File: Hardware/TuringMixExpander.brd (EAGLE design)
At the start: 99 x 50.3 mm, 35 parts, among them IC1 TL074P, IC2 TL072P

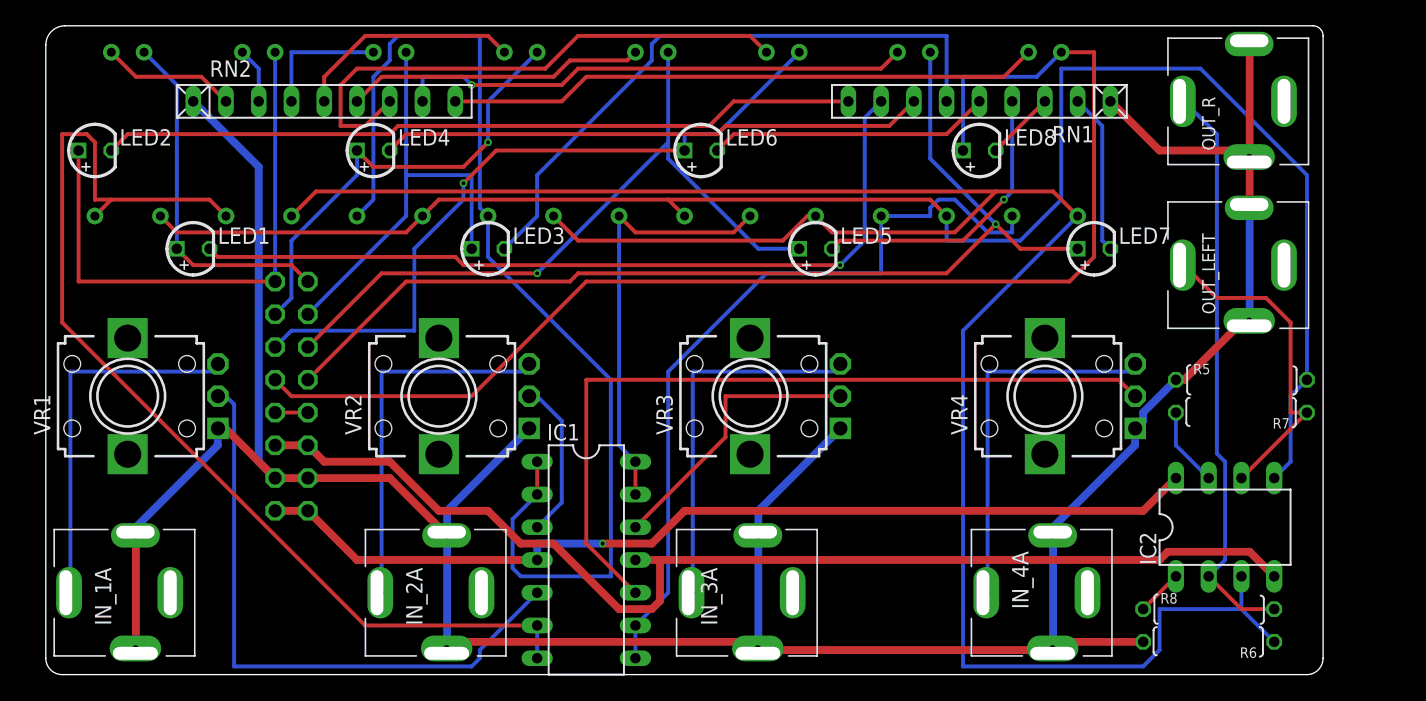
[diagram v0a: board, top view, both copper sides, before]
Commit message: New pcb layout
Added passthrough header
Removed resistor networks
Simplified led/resistor structure (one per channel, not two)
New panel layout
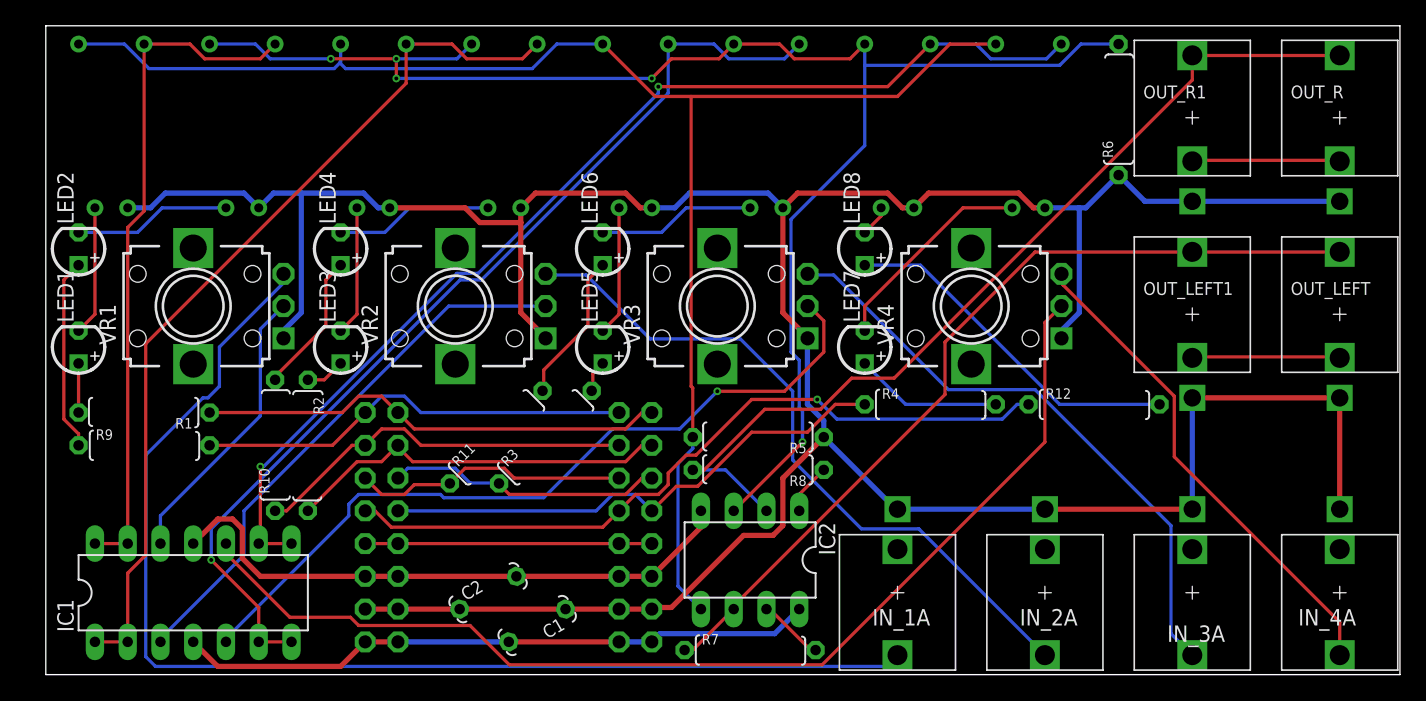
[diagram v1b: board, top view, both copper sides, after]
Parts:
- removed RN1, RN2: 2.2k, resistor-net:RN-9
- added C1, C2: 100n, TomW:C050-024X044
- added GATES1: (no value), con-lstb:MA08-2
- added OUT_LEFT1, OUT_R1: THONKICONN, TomW:THONKICONN
- added R1, R10, R11, R12, R2, R3, R4, R9: 2K, TomW:0207/10
- IN_1A, IN_2A, IN_3A, IN_4A, OUT_LEFT, OUT_R: value ERTHENVAR_SLIMLINE -> THONKICONN; device TomW:ERTHENVAR_SLIMLINE -> TomW:THONKICONN
- moved IN_1A 59.7 mm to (66.0, 6.35), turned to 180 degrees
- moved IN_2A 47.0 mm to (77.5, 6.35), turned to 180 degrees
- moved R7 42.3 mm to (54.6, 1.91), turned to 0 degrees
- moved R6 41.9 mm to (83.2, 43.8), turned to 90 degrees
- moved R5 37.7 mm to (55.2, 18.4), turned to 180 degrees
- moved IC2 36.9 mm to (54.6, 8.89), turned to 180 degrees
- moved R8 36.6 mm to (55.2, 15.9), turned to 180 degrees
- moved IN_3A 34.3 mm to (88.9, 6.35), turned to 180 degrees
- moved IC1 30.6 mm to (11.4, 6.35), turned to 0 degrees
- moved GATES 28.5 mm to (45.7, 11.4)
- moved IN_4A 22.9 mm to (100.3, 6.35), turned to 180 degrees
- moved LED7 19.3 mm to (63.5, 25.4), turned to 90 degrees
- moved LED5 18.2 mm to (43.2, 25.4), turned to 90 degrees
- moved LED3 13.7 mm to (22.9, 25.4), turned to 90 degrees
- moved LED1 11.7 mm to (2.54, 25.4), turned to 90 degrees
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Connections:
- removed net GR1: LDR1.1, RN2.2
- removed net GR2: LDR2.1, RN2.4
- removed net GR3: LDR3.1, RN2.6
- removed net GR4: LDR4.1, RN2.8
- removed net GR5: LDR5.1, RN2.3
- removed net GR6: LDR6.1, RN2.5
- removed net GR7: LDR7.1, RN2.7
- removed net GR8: LDR8.1, RN2.9
- new net N$14: LDR1.2, LED1.K
- new net N$24: OUT_R.P$2, OUT_R1.P$2
- new net N$25: LED1.A, R1.2
- new net N$26: LED3.A, R2.1
- new net N$27: LED5.A, R3.2
- new net N$28: LED7.A, R4.2
- new net N$29: LED2.A, R9.1
- new net N$30: LED4.A, R10.2
- new net N$31: LED6.A, R11.2
- new net N$32: LED8.A, R12.2
- net +12V: now also C1.2, GATES1.15, GATES1.16
- net -12V: now also C2.2, GATES1.11, GATES1.12
- net CLOCK: now also GATES1.10, GATES1.9
- net GATE1: now also GATES1.1, R1.1; no longer LDR1.2, LED1.A
- net GATE2: now also GATES1.2, R9.2; no longer LDR5.2, LED2.A
- net GATE3: now also GATES1.3, R2.2; no longer LDR2.2, LED3.A
- net GATE4: now also GATES1.4, R10.1; no longer LDR6.2, LED4.A
- net GATE5: now also GATES1.5, R3.1; no longer LDR3.2, LED5.A
- net GATE6: now also GATES1.6, R11.1; no longer LDR7.2, LED6.A
- net GATE7: now also GATES1.7, R4.1; no longer LDR4.2, LED7.A
- net GATE8: now also GATES1.8, R12.1; no longer LDR8.2, LED8.A
- net GND: now also C1.1, C2.1, GATES1.13, GATES1.14, IN_1A.P$1, IN_2A.P$1, IN_3A.P$1, IN_4A.P$1, LDR1.1, LDR2.1, LDR3.1, LDR4.1, LDR5.1, LDR6.1, LDR7.1, LDR8.1, OUT_LEFT.P$1, OUT_LEFT1.P$1, OUT_R.P$1, OUT_R1.P$1, R6.1; no longer IN_1A.GND1, IN_1A.GND2, IN_2A.GND1, IN_2A.GND2, IN_3A.GND1, IN_3A.GND2, IN_4A.GND1, IN_4A.GND2, OUT_LEFT.GND1, OUT_LEFT.GND2, OUT_R.GND1, OUT_R.GND2, R6.2, RN1.1, RN2.1
- net INPUT1: now also IC1.13, IC1.14; no longer IC1.6, IC1.7
- net INPUT3: now also IC1.6, IC1.7; no longer IC1.13, IC1.14
- net N$1: now also IN_1A.P$3; no longer IN_1A.TIP
- net N$10: now also OUT_R.P$3, OUT_R1.P$3; no longer OUT_R.TIP
- net N$11: now also IC1.5; no longer IC1.12
- net N$12: now also IN_3A.P$3; no longer IN_3A.TIP
- net N$13: now also IN_4A.P$3; no longer IN_4A.TIP
- net N$15: now also LDR2.2, LED3.K; no longer LED1.K, RN1.8
- net N$16: now also LDR3.2, LED5.K; no longer LED2.K, RN1.9
- net N$17: now also LDR4.2, LED7.K; no longer LED3.K, RN1.6
- net N$18: now also LDR5.2, LED2.K; no longer LED4.K, RN1.7
- net N$19: now also LDR6.2, LED4.K; no longer LED5.K, RN1.4
- net N$2: now also IC1.12; no longer IC1.5
- net N$20: now also LDR7.2; no longer RN1.5
- net N$21: now also LDR8.2, LED8.K; no longer LED7.K, RN1.2
- net N$22: now also OUT_LEFT.P$2, OUT_LEFT1.P$2; no longer LED8.K, RN1.3
- net N$3: now also IN_2A.P$3; no longer IN_2A.TIP
- net N$7: now also OUT_LEFT.P$3, OUT_LEFT1.P$3; no longer OUT_LEFT.TIP
- net SUMR: now also R6.2; no longer R6.1
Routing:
- net N$1: track 29.3 -> 93.4 mm
- net N$15: track 63.4 -> 10.1 mm, vias 1 -> 0
- net N$16: track 58.7 -> 10.1 mm
- net SUMR: track 170.3 -> 122.7 mm, vias 0 -> 5
- net GR8: track 46.0 -> 0.00 mm
- net INPUT3: track 33.3 -> 77.2 mm, vias 0 -> 1
- net GATE8: track 101.0 -> 57.7 mm, vias 0 -> 1
- net -12V: track 89.1 -> 46.2 mm
- net GR7: track 42.9 -> 0.00 mm
- net N$7: track 25.6 -> 66.1 mm
- net GATE7: track 80.9 -> 40.7 mm, vias 1 -> 0
- net GR4: track 40.1 -> 0.00 mm, vias 1 -> 0
- net N$11: track 22.0 -> 60.7 mm, vias 0 -> 1
- net GATE5: track 55.8 -> 21.4 mm, vias 1 -> 0
- net GATE6: track 55.3 -> 21.4 mm, vias 1 -> 0
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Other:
- board size 99 x 50.3 mm -> 105 x 50.3 mm
- board text added: "Turing Machine Expander 3 Vactrol Matrix Mixer Designed by Tom Whitwell In Herne Hill, London, Feb 2015 PCB Rev 3"
- board text removed: "Turing Machine Expander 3 Vactrol Matrix Mixer Designed by Tom Whitwell In Herne Hill, London, May 2013 PCB Rev 2"

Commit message: New resistor grid
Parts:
- R1, R10, R11, R12, R2, R3, R4, R5, R6, R7, R8, R9: device TomW:0207/10 -> TomW:0207/7
- moved R6 24.5 mm to (76.2, 20.3), turned to 180 degrees
- moved R12 15.3 mm to (66.0, 20.3)
- moved R4 4.07 mm to (66.0, 17.8)
- moved IC1 4.02 mm to (12.7, 10.2)
- moved R11 3.24 mm to (38.1, 19.1), turned to 90 degrees
- moved R10 2.54 mm to (17.8, 20.3), turned to 180 degrees
- moved R2 2.54 mm to (17.8, 17.8), turned to 0 degrees
- moved R3 2.01 mm to (40.6, 19.1), turned to 90 degrees
- moved R5 2.01 mm to (54.6, 20.3)
- moved R8 2.01 mm to (54.6, 17.8)
- moved R1 1.27 mm to (6.35, 20.3), turned to 0 degrees
- moved R9 1.27 mm to (6.35, 17.8)
- moved R7 1.27 mm to (54.6, 3.17)
- moved IC2 1.27 mm to (54.6, 10.2)
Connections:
- net GATE1: now also R1.2; no longer R1.1
- net N$25: now also R1.1; no longer R1.2
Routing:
- net INPUT3: track 77.2 -> 115.9 mm, vias 1 -> 2
- net N$23: track 86.1 -> 119.4 mm, vias 0 -> 1
- net N$26: track 3.07 -> 27.0 mm
- net INPUT4: track 85.4 -> 107.9 mm, vias 2 -> 1
- net GND: track 257.5 -> 278.8 mm
- net N$1: track 93.4 -> 75.5 mm, vias 0 -> 1
- net N$4: track 42.8 -> 59.4 mm
- net GATE8: track 57.7 -> 42.4 mm, vias 1 -> 0
- net N$3: track 54.1 -> 68.8 mm
- net N$32: track 27.3 -> 14.1 mm
- net INPUT2: track 68.9 -> 77.2 mm, vias 0 -> 2
- net N$30: track 11.0 -> 18.8 mm, vias 0 -> 1
- net SUMR: track 122.7 -> 115.8 mm, vias 5 -> 2
- net N$13: track 38.5 -> 44.9 mm
- net -12V: track 46.2 -> 51.6 mm
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
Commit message: PCB work
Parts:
- added U$1: (no value), TW_logos:MTM_2CM
- added U$2: (no value), TW_logos:CC_1CM_SCREENPRINT
- added U$3: (no value), TW_logos:THONK_1CM_SCREENPRINT
- moved R3 20.4 mm to (20.3, 17.8), turned to 180 degrees
- moved R11 17.8 mm to (20.3, 20.3), turned to 180 degrees
- moved R10 14.5 mm to (26.7, 8.89)
- moved GATES1 13.6 mm to (36.8, 3.17), turned to 180 degrees
- moved GATES 11.7 mm to (36.8, 19.1), turned to 180 degrees
- moved R2 10.2 mm to (26.7, 12.7)
- moved C1 9.92 mm to (44.5, 11.4), turned to 300 degrees
- moved C2 8.52 mm to (41.9, 10.2), turned to 120 degrees
- moved IN_1A 2.54 mm to (66.0, 8.89)
- moved IN_2A 2.54 mm to (77.5, 8.89)
- moved IN_3A 2.54 mm to (88.9, 8.89)
- moved IN_4A 2.54 mm to (100.3, 8.89)
- moved IC1 1.80 mm to (11.4, 8.89)
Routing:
- net N$27: track 3.07 -> 48.7 mm
- net N$23: track 119.4 -> 83.8 mm, vias 1 -> 0
- net GND: track 278.8 -> 250.0 mm
- net INPUT3: track 115.9 -> 89.7 mm, vias 2 -> 3
- net N$31: track 11.7 -> 34.2 mm, vias 0 -> 1
- net N$7: track 68.8 -> 88.2 mm
- net +12V: track 49.8 -> 68.3 mm
- net N$1: track 75.5 -> 92.7 mm, vias 1 -> 0
- net N$3: track 68.8 -> 51.7 mm, vias 0 -> 1
- net N$26: track 27.0 -> 11.4 mm
- net N$10: track 73.1 -> 86.3 mm
- net N$11: track 65.6 -> 77.0 mm, vias 1 -> 0
- net GATE7: track 39.2 -> 50.1 mm
- net -12V: track 51.6 -> 60.8 mm
- net GATE3: track 27.5 -> 18.7 mm
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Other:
- board text added: "EXPANDER ONLY Do not connect to power Connect to GATES Use either header"
- board text removed: "EXPANDER ONLY Do not connect to power header"
